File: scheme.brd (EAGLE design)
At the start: 100 x 80 mm, 34 parts, among them J1 22-05-7048-04, J2 22-05-7028-02

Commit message: Minor fix of routes
Signed-off-by: Nikita 'webconn' Maslov <wkernelteam@gmail.com>
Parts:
- R10, R9: device rcl:R1206 -> resistor:R0805
- moved R9 2.03 mm to (41.9, 37.1), turned to 180 degrees
- moved R10 1.59 mm to (41.9, 34.6), turned to 0 degrees
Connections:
- net PB5: now also R10.1; no longer R9.2
- net VCC: now also R9.2; no longer R10.1
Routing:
- net VCC: track 307.5 -> 312.1 mm
- net PB5: track 28.5 -> 31.1 mm
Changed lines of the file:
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@@
 <element name="JP2" library="SparkFun-Connectors" package="1X06" value="" x="95.25" y="69.215" rot="R270"/>
 <element name="JP3" library="SparkFun-Connectors" package="1X06" value="" x="97.79" y="69.215" rot="R270"/>
-<element name="R9" library="rcl" package="R1206" value="0" x="40.3225" y="35.8775" rot="MR270"/>
-<element name="R10" library="rcl" package="R1206" value="0" x="42.8625" y="35.8775" rot="MR90"/>
 <element name="J2" library="con-molex" package="7395-02" value="22-05-7028-02" x="52.705" y="7.3025" rot="R90">
 <attribute name="OC_NEWARK" value="unknown" x="52.705" y="7.3025" size="1.778" layer="27" rot="R90" display="off"/>
@@
 <attribute name="OC_FARNELL" value="9731601" x="52.705" y="7.3025" size="1.778" layer="27" rot="R90" display="off"/>
 </element>
+<element name="R9" library="resistor" package="R0805" value="0" x="41.91" y="37.1475" rot="MR180"/>
+<element name="R10" library="resistor" package="R0805" value="0" x="41.91" y="34.6075" rot="MR0"/>
 </elements>
 <signals>
@@
 <wire x1="34.29" y1="17.145" x2="31.75" y2="14.605" width="0.4064" layer="16"/>
 <contactref element="JP4" pad="2"/>
-<contactref element="R10" pad="1"/>
-<wire x1="42.8625" y1="34.4555" x2="42.8625" y2="30.48" width="0.4064" layer="16"/>
-<wire x1="42.8625" y1="30.48" x2="42.2275" y2="29.845" width="0.4064" layer="16"/>
 <wire x1="17.78" y1="17.78" x2="20.0025" y2="17.78" width="0.4064" layer="16"/>
 <wire x1="20.0025" y1="17.78" x2="21.59" y2="16.1925" width="0.4064" layer="16"/>
@@
 <wire x1="19.05" y1="29.5275" x2="17.78" y2="29.5275" width="0.4064" layer="16"/>
 <wire x1="17.78" y1="29.5275" x2="17.62125" y2="29.68625" width="0.4064" layer="16"/>
+<contactref element="R9" pad="2"/>
+<wire x1="42.76" y1="37.1475" x2="43.815" y2="37.1475" width="0.4064" layer="16"/>
+<wire x1="43.815" y1="37.1475" x2="44.45" y2="36.5125" width="0.4064" layer="16"/>
+<wire x1="44.45" y1="36.5125" x2="44.45" y2="32.0675" width="0.4064" layer="16"/>
+<wire x1="44.45" y1="32.0675" x2="42.2275" y2="29.845" width="0.4064" layer="16"/>
 </signal>
 <signal name="N$4">
@@
 <wire x1="31.4325" y1="35.56" x2="33.655" y2="33.3375" width="0.4064" layer="16"/>
 <wire x1="33.655" y1="33.3375" x2="37.1475" y2="33.3375" width="0.4064" layer="16"/>
-<contactref element="R9" pad="2"/>
-<wire x1="37.1475" y1="33.3375" x2="40.005" y2="33.3375" width="0.4064" layer="16"/>
-<wire x1="40.005" y1="33.3375" x2="40.3225" y2="33.655" width="0.4064" layer="16"/>
-<wire x1="40.3225" y1="33.655" x2="40.3225" y2="34.4555" width="0.4064" layer="16"/>
+<wire x1="37.1475" y1="33.3375" x2="42.2275" y2="33.3375" width="0.4064" layer="16"/>
+<contactref element="R10" pad="1"/>
+<wire x1="42.2275" y1="33.3375" x2="42.8625" y2="33.9725" width="0.4064" layer="16"/>
+<wire x1="42.8625" y1="33.9725" x2="42.8625" y2="34.505" width="0.4064" layer="16"/>
+<wire x1="42.8625" y1="34.505" x2="42.76" y2="34.6075" width="0.4064" layer="16"/>
 </signal>
 <signal name="PB4">
@@
 <wire x1="22.225" y1="29.21" x2="22.225" y2="19.3675" width="0.8128" layer="16"/>
 <wire x1="22.225" y1="19.3675" x2="22.86" y2="18.7325" width="0.8128" layer="16"/>
-<wire x1="22.86" y1="18.7325" x2="26.9875" y2="18.7325" width="0.8128" layer="16"/>
-<via x="26.9875" y="18.7325" extent="1-16" drill="0.6" diameter="1.4224" shape="octagon"/>
-<wire x1="26.9875" y1="18.7325" x2="45.4025" y2="18.7325" width="0.8128" layer="1"/>
+<wire x1="22.86" y1="18.7325" x2="29.21" y2="18.7325" width="0.8128" layer="16"/>
+<via x="29.21" y="18.7325" extent="1-16" drill="0.6" diameter="1.4224" shape="octagon"/>
+<wire x1="29.21" y1="18.7325" x2="45.4025" y2="18.7325" width="0.8128" layer="1"/>
 <via x="45.4025" y="18.7325" extent="1-16" drill="0.6" diameter="1.4224" shape="octagon"/>
 <wire x1="45.4025" y1="18.7325" x2="47.9425" y2="18.7325" width="0.8128" layer="16"/>
@@
 <signal name="N$17">
 <contactref element="JP5" pad="1"/>
+<wire x1="37.1475" y1="38.4175" x2="40.005" y2="38.4175" width="0.4064" layer="16"/>
 <contactref element="R9" pad="1"/>
 <contactref element="R10" pad="2"/>
-<wire x1="37.1475" y1="38.4175" x2="40.005" y2="38.4175" width="0.4064" layer="16"/>
-<wire x1="40.005" y1="38.4175" x2="40.3225" y2="38.1" width="0.4064" layer="16"/>
-<wire x1="40.3225" y1="38.1" x2="40.3225" y2="37.2995" width="0.4064" layer="16"/>
-<wire x1="40.3225" y1="37.2995" x2="42.8625" y2="37.2995" width="0.4064" layer="16"/>
+<wire x1="40.005" y1="38.4175" x2="41.06" y2="37.3625" width="0.4064" layer="16"/>
+<wire x1="41.06" y1="37.3625" x2="41.06" y2="37.1475" width="0.4064" layer="16"/>
+<wire x1="41.06" y1="37.1475" x2="41.06" y2="34.6075" width="0.4064" layer="16"/>
 </signal>
 </signals>

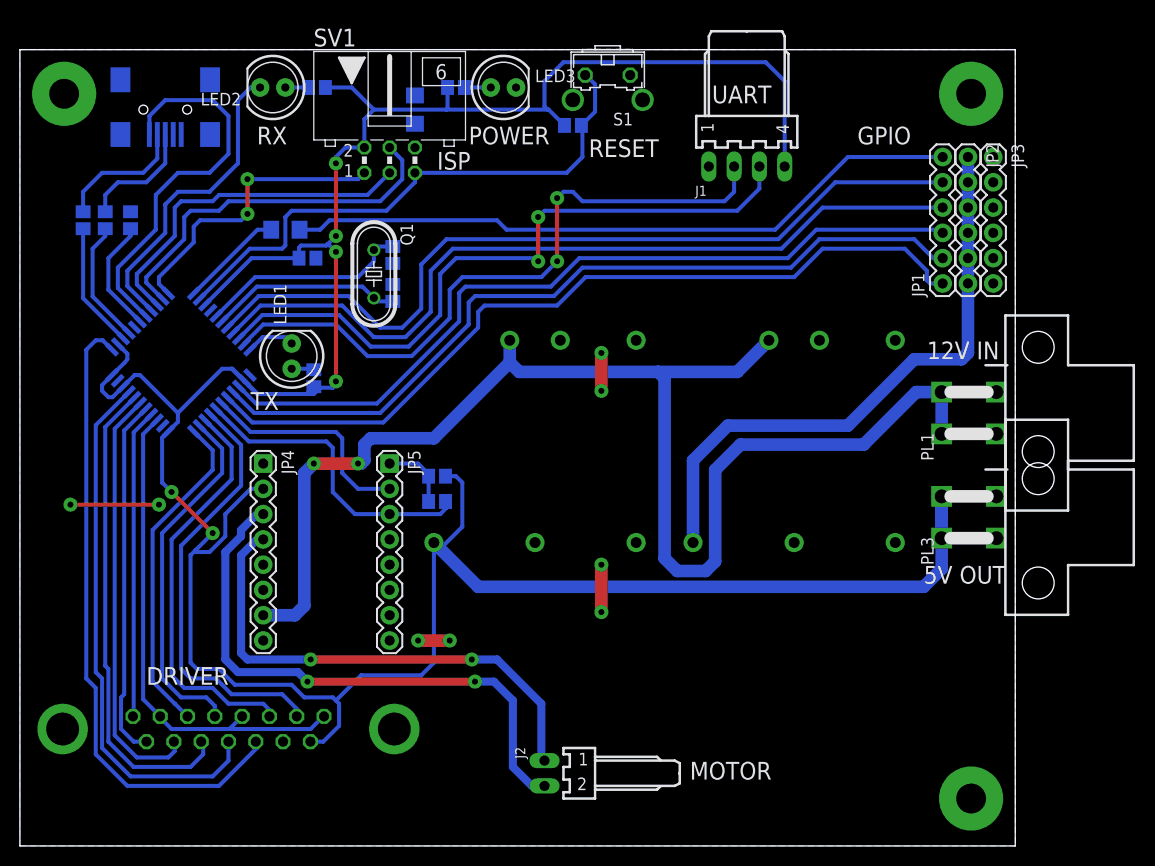
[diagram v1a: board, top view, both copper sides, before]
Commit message: Add BOOT button and fix isolation
Signed-off-by: Nikita 'webconn' Maslov <wkernelteam@gmail.com>
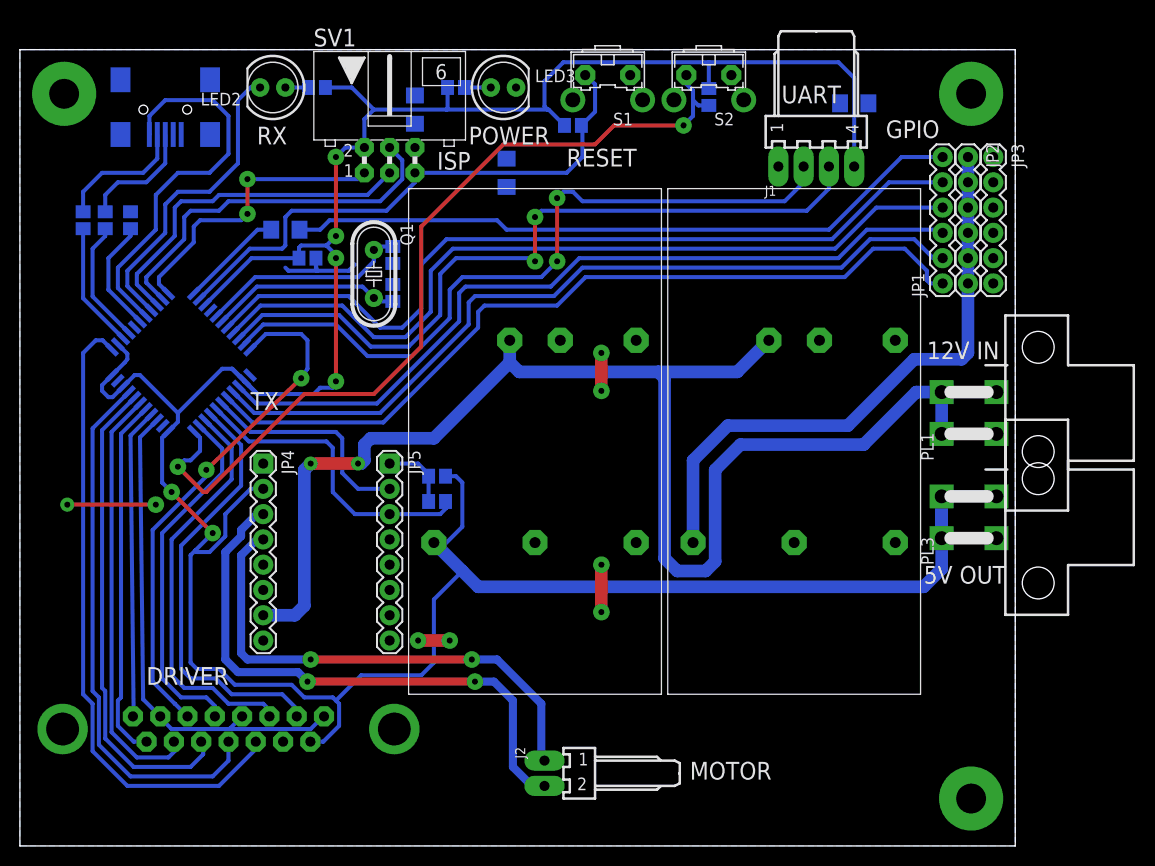
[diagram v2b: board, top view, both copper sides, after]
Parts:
- removed LED1: (no value), SparkFun-LED:LED5MM
- added R11, R12: 0, rcl:R1206
- added S2: (no value), switch-omron:B3F-31XX
- R4: value 300 -> 10K
- moved R4 48.7 mm to (69.2, 75.2), turned to 90 degrees
- moved U$3 26.0 mm to (51.8, 40.6), flipped to the top, turned to 90 degrees
- moved U$4 26.0 mm to (77.8, 40.6), flipped to the top, turned to 90 degrees
- moved J1 6.98 mm to (80.0, 68.3)
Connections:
- net RXLED renamed LED
- removed net N$12: LED1.A, R4.1
- removed net TXLED: LED1.K, U$1.22
- new net HWB: R4.1, S2.2, U$1.33
- net +5V: now also U$4.3; no longer U$3.3
- net GND: now also R11.1, R11.2, R12.1, R12.2, S2.1
- net RELAY: now also U$1.22; no longer U$1.33
- net VCC: now also U$3.3; no longer U$4.3
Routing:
- net HWB: track 0.00 -> 86.8 mm, vias 0 -> 2
- net RELAY: track 33.4 -> 52.4 mm, vias 0 -> 2
- net GND: track 20.6 -> 29.9 mm
- net VCC: track 312.1 -> 319.1 mm
- net RXD: track 68.7 -> 75.7 mm
- net TXD: track 66.9 -> 73.4 mm
- net TXLED: track 5.16 -> 0.00 mm
- net N$12: track 2.26 -> 0.00 mm
